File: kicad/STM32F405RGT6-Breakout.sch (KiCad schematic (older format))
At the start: 51 parts, among them J1 USB_C_Receptacle_USB2.0, J2 PWR OUT, J3 SWD/JTAG, J4 USART6, J5 SPI1, J6 I2C1, J7 I2C2, Q1 Si2301CDS, U1 STM32F405RGT6, U2 AMS1117-3.3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

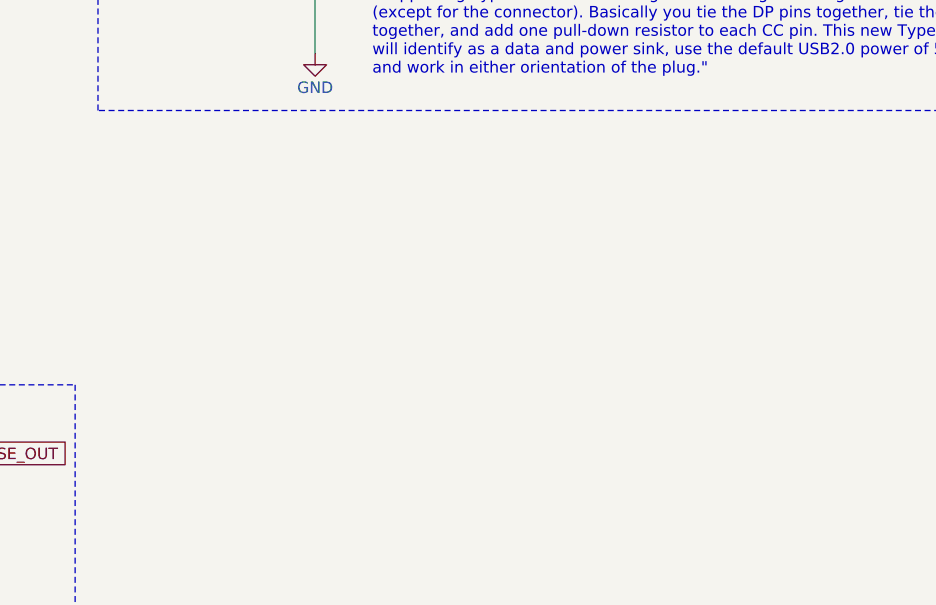
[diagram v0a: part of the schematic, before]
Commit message: clarify what software the board files are for
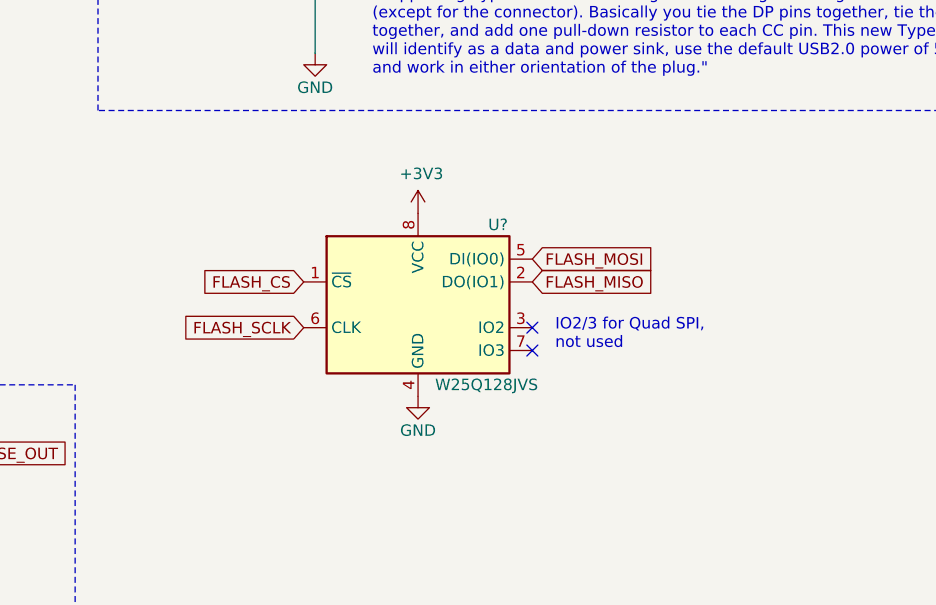
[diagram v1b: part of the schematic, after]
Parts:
- added U?: W25Q128JVS, Package_SO:SOIC-8_5.23x5.23mm_P1.27mm, symbol Memory_Flash:W25Q128JVS
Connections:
- net labels added: FLASH_CS, FLASH_MISO, FLASH_MOSI, FLASH_SCLK
- no-connect marks 37 -> 39
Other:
- note added: "IO2/3 for Quad SPI,\nnot used"
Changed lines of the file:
@@
 Wire Wire Line
 	2500 1350 2900 1350
+$Comp
+L Memory_Flash:W25Q128JVS U?
+U 1 1 61978862
+P 7500 6050
+F 0 "U?" H 7850 6400 50  0000 C CNN
+F 1 "W25Q128JVS" H 7800 5700 50  0000 C CNN
+F 2 "Package_SO:SOIC-8_5.23x5.23mm_P1.27mm" H 7500 6050 50  0001 C CNN
+F 3 "http://www.winbond.com/resource-files/w25q128jv_dtr%20revc%2003272018%20plus.pdf" H 7500 6050 50  0001 C CNN
+	1    7500 6050
+	1    0    0    -1
+$EndComp
+$Comp
+L power:GND #PWR?
+U 1 1 6197D247
+P 7500 6450
+F 0 "#PWR?" H 7500 6200 50  0001 C CNN
+F 1 "GND" H 7500 6300 50  0000 C CNN
+F 2 "" H 7500 6450 50  0001 C CNN
+F 3 "" H 7500 6450 50  0001 C CNN
+	1    7500 6450
+	1    0    0    -1
+$EndComp
+$Comp
+L power:+3V3 #PWR?
+U 1 1 6197DBCF
+P 7500 5650
+F 0 "#PWR?" H 7500 5500 50  0001 C CNN
+F 1 "+3V3" H 7515 5823 50  0000 C CNN
+F 2 "" H 7500 5650 50  0001 C CNN
+F 3 "" H 7500 5650 50  0001 C CNN
+	1    7500 5650
+	1    0    0    -1
+$EndComp
+Text GLabel 7000 5950 0    50   Input ~ 0
+FLASH_CS
+Text GLabel 7000 6150 0    50   Input ~ 0
+FLASH_SCLK
+Text GLabel 8000 5850 2    50   Input ~ 0
+FLASH_MOSI
+Text GLabel 8000 5950 2    50   Input ~ 0
+FLASH_MISO
+NoConn ~ 8000 6150
+NoConn ~ 8000 6250
+Text Notes 8100 6250 0    50   ~ 0
+IO2/3 for Quad SPI,\nnot used
 $EndSCHEMATC

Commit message: - Added onboard SPI flash, just to experiment with (128mb NOR flash is basic part at JLCPCB) - Added momentary switches for BOOT0 and NRST to get into DFU mode, like the black pill - Added a capacitor on NRST to avoid parasitic resets
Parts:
- removed R7: 10k, symbol Device:R_Small
- added C?: 0.1u, symbol Device:C_Small
- added C?: 4.7u, Capacitor_SMD:C_0805_2012Metric, symbol Device:C_Small
- added C?: 0.1u, Capacitor_SMD:C_0603_1608Metric, symbol Device:C_Small
- added R? (x6): 10k, symbol Device:R_Small
- added SW?: BOOT0 Momentary, symbol Switch:SW_Push_SPDT
- added SW?: NRST Momentary, symbol Switch:SW_Push_SPDT
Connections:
- net labels added: FLASH_SCK
- net labels removed: FLASH_SCLK
- wire segments 134 -> 153
- no-connect marks 39 -> 34
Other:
- note added: "(internal pullup)"
- note added: "Boot mode selection\n"
- note added: "Power supply"
- note added: "Quad\nSPI\nnot\nused"
- note added: "SPI Flash"
- note removed: "IO2/3 for Quad SPI,\nnot used"
- note removed: "Set boot mode"
- moved on the sheet: C14, C15, FB2, R3, R4, R5, R6, R8, U?

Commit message: Half way done with footprint assignment
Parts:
- removed F1: 500mA, symbol Device:Fuse_Small
- added F?: 500mA, symbol Device:Polyfuse_Small
- C16: footprint (none) -> Capacitor_SMD:C_1206_3216Metric
- C17: footprint (none) -> Capacitor_SMD:C_0805_2012Metric
- C18: renamed from C?; value 0.1u -> 100n; footprint (none) -> Capacitor_SMD:C_0402_1005Metric
- C19: renamed from C?; value 0.1u -> 100n
- D1: footprint (none) -> Diode_SMD:D_MiniMELF
- D2, D3: footprint (none) -> Diode_SMD:D_0603_1608Metric
- FB1, FB2: footprint (none) -> Inductor_SMD:L_0805_2012Metric
- H1, H2, H3, H4: footprint MountingHole:MountingHole_3mm_Pad_Via -> MountingHole:MountingHole_4.3mm_M4_Pad_Via
- J2: footprint (none) -> Connector_PinHeader_2.54mm:PinHeader_1x02_P2.54mm_Vertical_SMD_Pin1Left
- J3: footprint (none) -> Connector_PinSocket_1.27mm:PinSocket_2x05_P1.27mm_Vertical_SMD
- J4, J5, J6, J7: footprint (none) -> Connector_PinHeader_2.54mm:PinHeader_1x04_P2.54mm_Vertical_SMD_Pin1Left
- gave numbers to parts that had none: 10
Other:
- note removed: "Fuse\n(does this go \nbefore or \nafter pch?)"
- moved on the sheet: D1, Q1, R1

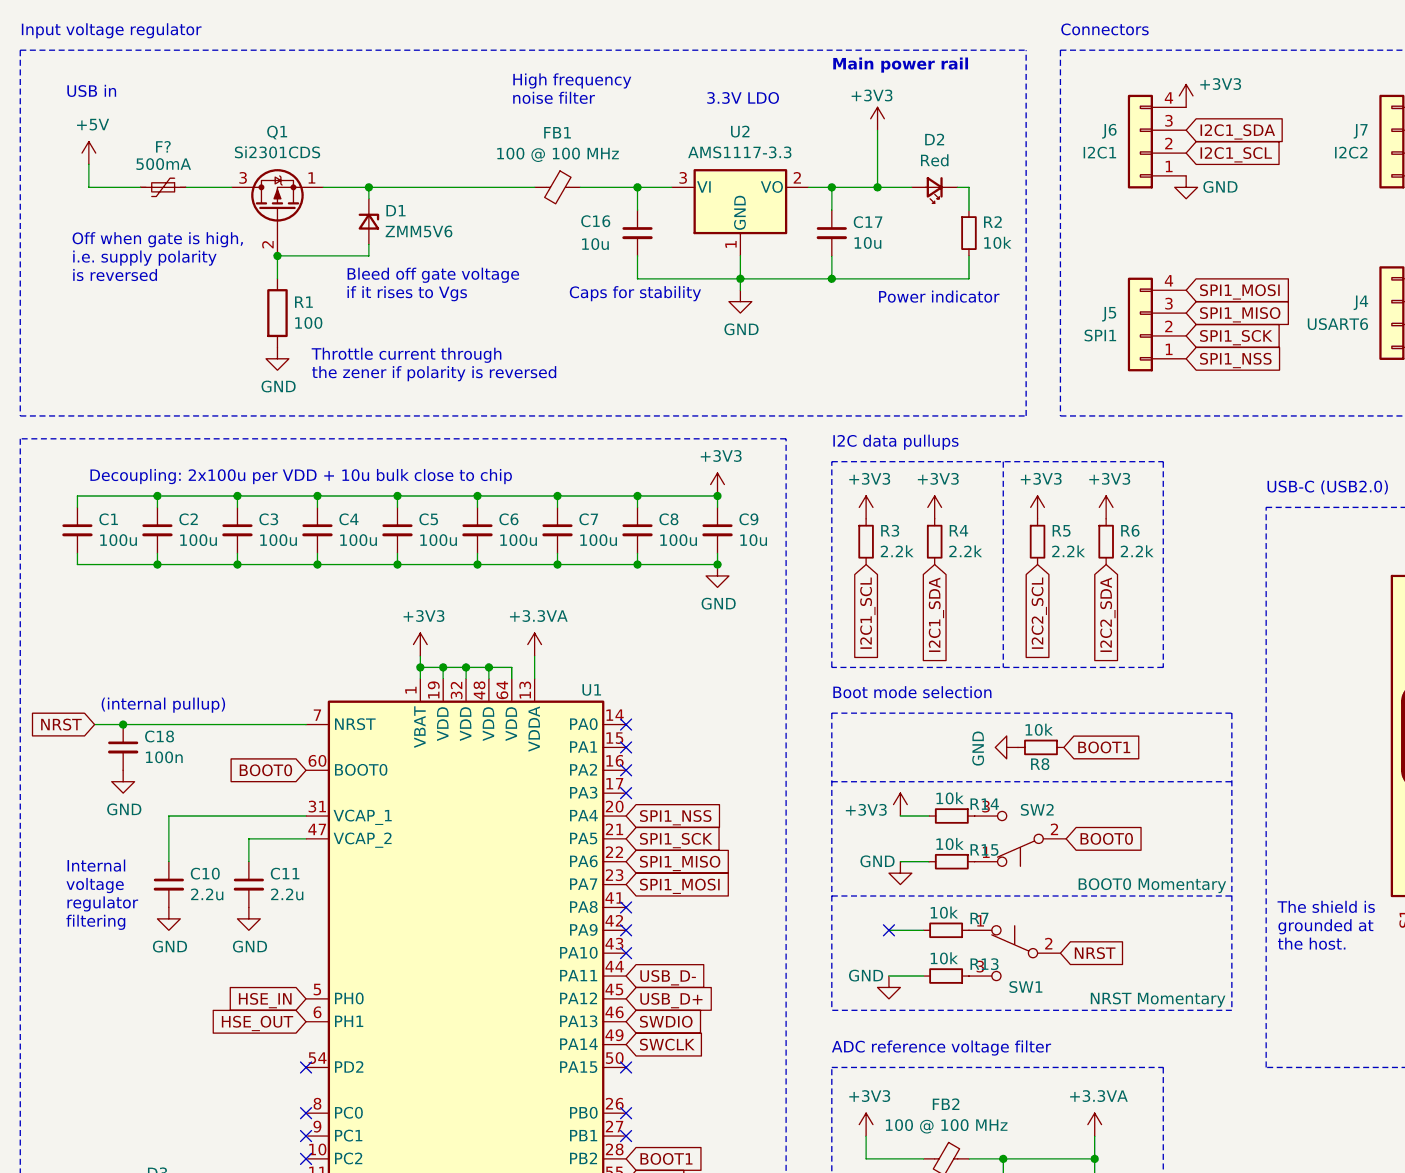
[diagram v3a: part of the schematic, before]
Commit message: - Added SPST tact switch symbol & footprint from JLPCB - Used SPST to ground NRST for reset - Used SPST to raise BOOT0 for DFU - BOOT0 on voltage divider, should work with the switch bringing BOOT0 to >2.2V (min high level 1.88V)
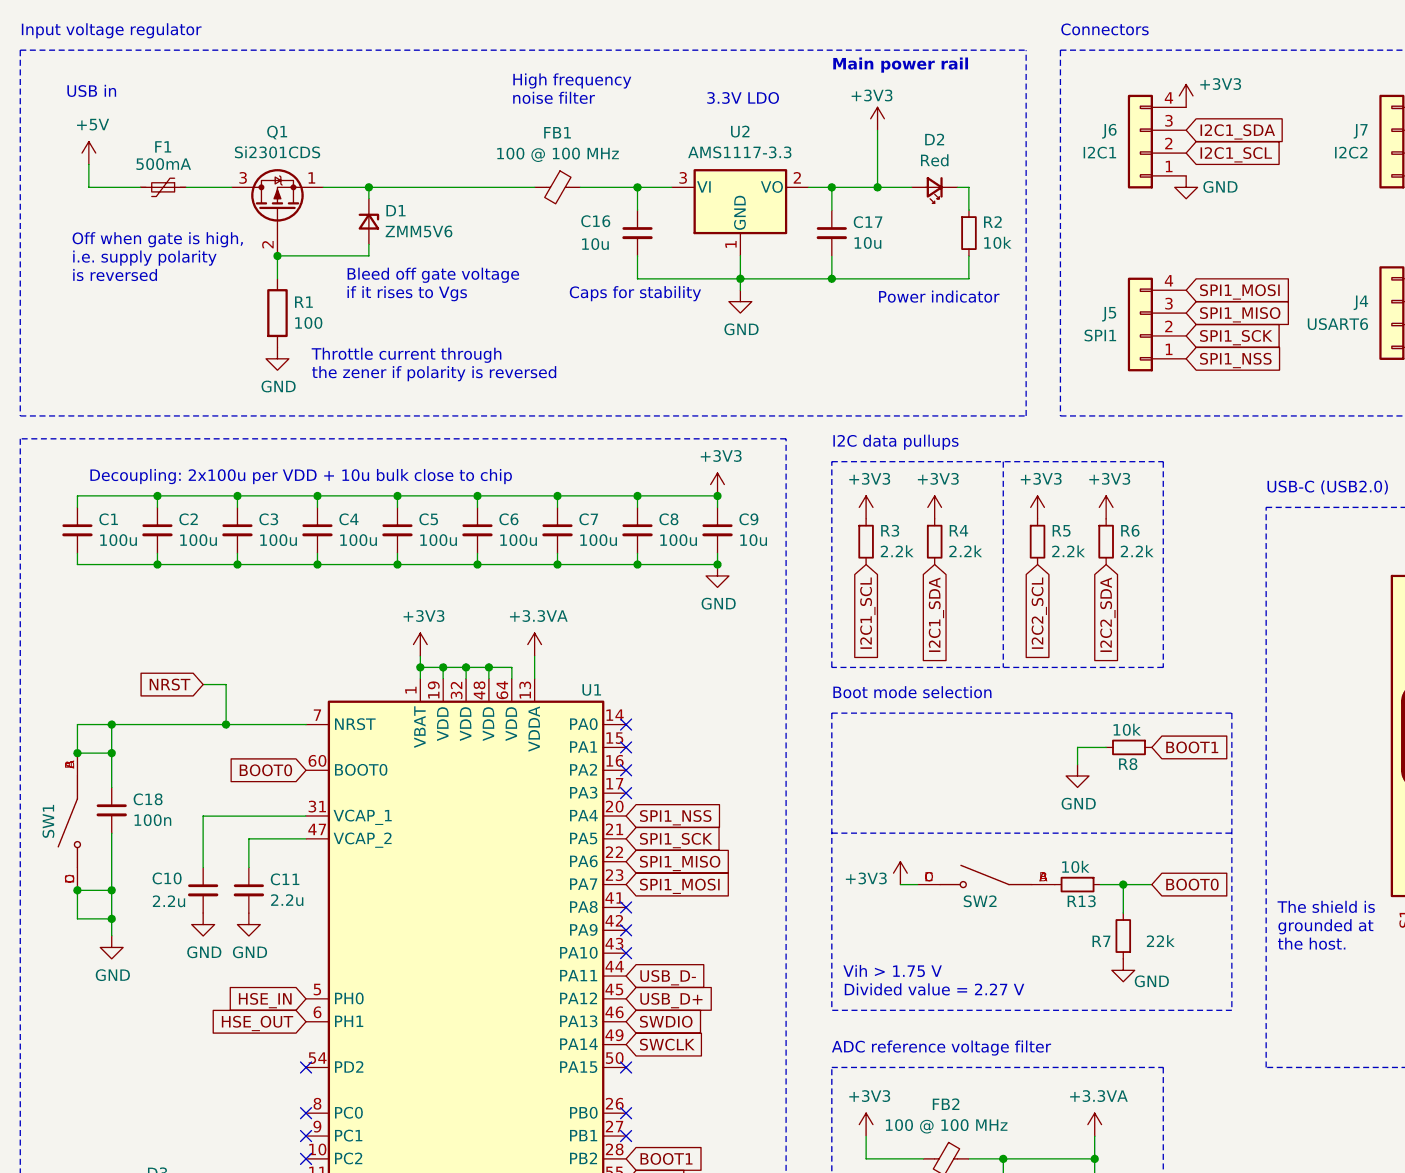
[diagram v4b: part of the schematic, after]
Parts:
- removed R14, R15: 10k, symbol Device:R_Small
- removed SW1: NRST Momentary, symbol Switch:SW_Push_SPDT
- removed SW2: BOOT0 Momentary, symbol Switch:SW_Push_SPDT
- added SW1, SW2: TS-1187A-B-A-B, TS-1187A-B-A-B:SW_TS-1187A-B-A-B, symbol TS-1187A-B-A-B:TS-1187A-B-A-B
- C1, C12, C13, C14, C15, C2, C3, C4, C5, C6, C7, C8: footprint (none) -> Capacitor_SMD:C_0402_1005Metric
- C10, C11, C9: footprint (none) -> Capacitor_SMD:C_0603_1608Metric
- C16: footprint Capacitor_SMD:C_1206_3216Metric -> Capacitor_SMD:C_0805_2012Metric
- F1: renamed from F?; footprint (none) -> Fuse:Fuse_0603_1608Metric
- FB1, FB2: JLCPCB Part (none) -> C1015
- HSE1: JLCPCB Part (none) -> C160456
- J1: JLCPCB Part (none) -> C319148
- Q1: footprint (none) -> Package_TO_SOT_SMD:SOT-23; JLCPCB Part (none) -> C10487
- R1: footprint (none) -> Resistor_SMD:R_0805_2012Metric
- R10, R11, R12, R13, R16, R17, R3, R4, R5, R6, R8: footprint (none) -> Resistor_SMD:R_0402_1005Metric
- R2, R9: footprint (none) -> Resistor_SMD:R_0603_1608Metric
- R7: value 10k -> 22k; footprint (none) -> Resistor_SMD:R_0603_1608Metric
- U1: JLCPCB Part (none) -> C15742
- U2: JLCPCB Part (none) -> C6186
- U3: JLCPCB Part (none) -> C2827654
- U4: JLCPCB Part (none) -> C97521
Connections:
- net +3V3: now also SW2.C, SW2.D
- net BOOT0: now also R13.1, R7.2
- net GND: now also R7.1, SW1.C, SW1.D; no longer R13.2
- net NRST: now also SW1.A, SW1.B
- new net: R13.2, SW2.A, SW2.B
- no-connect marks 34 -> 33
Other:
- note added: "Vih > 1.75 V\nDivided value = 2.27 V"
- note removed: "(internal pullup)"
- note removed: "Internal\nvoltage\nregulator\nfiltering"
- moved on the sheet: C10, C11, C18, R8

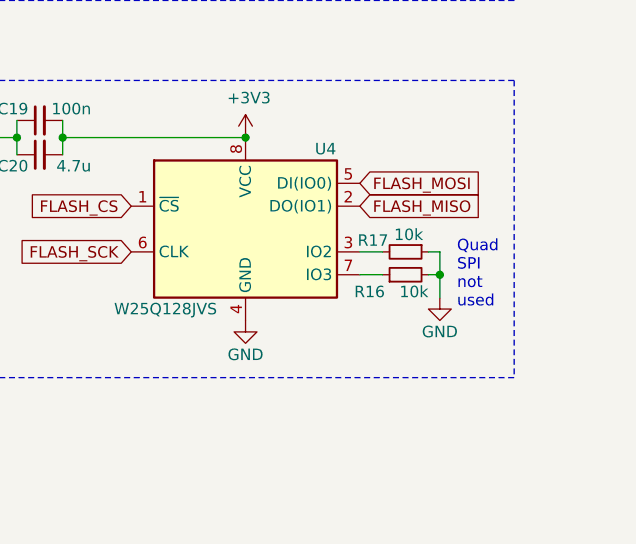
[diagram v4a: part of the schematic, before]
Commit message: - Laid out & routed crystal - Laid out & started routing MCU decoupling
--> Checkpoint before trying new flash orientation
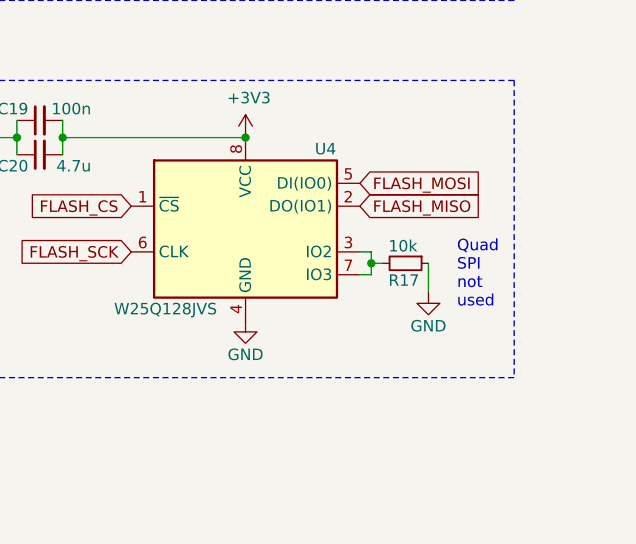
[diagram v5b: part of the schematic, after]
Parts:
- removed R16: 10k, Resistor_SMD:R_0402_1005Metric, symbol Device:R_Small
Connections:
- net GND: now also R17.1; no longer R17.2
- net at U4.3 (IO2): now also R17.2, U4.7 (IO3)
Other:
- moved on the sheet: R17
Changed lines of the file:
@@
 Quad\nSPI\nnot\nused
-$Comp
-L Device:R_Small R16
-U 1 1 6199EE81
-P 10275 6300
-F 0 "R16" V 10450 6075 50  0000 L CNN
-F 1 "10k" V 10200 6250 50  0000 L CNN
-F 2 "Resistor_SMD:R_0402_1005Metric" H 10275 6300 50  0001 C CNN
-F 3 "~" H 10275 6300 50  0001 C CNN
-	1    10275 6300
-	0    1    1    0
-$EndComp
-Wire Wire Line
-	10075 6300 10175 6300
 $Comp
 L power:GND #PWR0104
 U 1 1 619AB58F
-P 10425 6500
-F 0 "#PWR0104" H 10425 6250 50  0001 C CNN
-F 1 "GND" H 10425 6350 50  0000 C CNN
-F 2 "" H 10425 6500 50  0001 C CNN
-F 3 "" H 10425 6500 50  0001 C CNN
-	1    10425 6500
+P 10375 6475
+F 0 "#PWR0104" H 10375 6225 50  0001 C CNN
+F 1 "GND" H 10375 6325 50  0000 C CNN
+F 2 "" H 10375 6475 50  0001 C CNN
+F 3 "" H 10375 6475 50  0001 C CNN
+	1    10375 6475
 	1    0    0    -1
 $EndComp
@@
 L Device:R_Small R17
 U 1 1 6199FF9F
-P 10275 6400
-F 0 "R17" V 10425 6475 50  0000 L CNN
-F 1 "10k" V 10200 6300 50  0000 L CNN
-F 2 "Resistor_SMD:R_0402_1005Metric" H 10275 6400 50  0001 C CNN
-F 3 "~" H 10275 6400 50  0001 C CNN
-	1    10275 6400
-	0    -1   -1   0
-$EndComp
-Wire Wire Line
-	10375 6300 10425 6300
-Wire Wire Line
-	10425 6300 10425 6400
-Wire Wire Line
-	10375 6400 10425 6400
-Connection ~ 10425 6400
-Wire Wire Line
-	10425 6400 10425 6500
-Wire Wire Line
-	10175 6400 10075 6400
+P 10275 6350
+F 0 "R17" V 10350 6275 50  0000 L CNN
+F 1 "10k" V 10200 6275 50  0000 L CNN
+F 2 "Resistor_SMD:R_0402_1005Metric" H 10275 6350 50  0001 C CNN
+F 3 "~" H 10275 6350 50  0001 C CNN
+	1    10275 6350
+	0    1    1    0
+$EndComp
 Wire Notes Line
 	10750 5550 10750 6850
@@
 Text Notes 4250 4900 0    50   ~ 0
 Vih > 1.75 V\nDivided value = 2.27 V
+Wire Wire Line
+	10075 6300 10125 6300
+Wire Wire Line
+	10075 6400 10125 6400
+Wire Wire Line
+	10375 6350 10375 6475
+Wire Wire Line
+	10125 6300 10125 6350
+Wire Wire Line
+	10125 6350 10175 6350
+Connection ~ 10125 6350
+Wire Wire Line
+	10125 6350 10125 6400
 $EndSCHEMATC

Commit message: - USB connector & ESD protection laid out - Crystal moved to make room for fanning out GPIO pins
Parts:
- removed R12: 5.1k, Resistor_SMD:R_0402_1005Metric, symbol Device:R_Small
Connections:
- net at J1.A5 (CC1), R11.2: now also J1.B5 (CC2)
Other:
- moved on the sheet: R11
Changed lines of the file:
@@
 "Supporting Type-C from an existing USB2.0 design is straightforward and cheap \n(except for the connector). Basically you tie the DP pins together, tie the DM pins \ntogether, and add one pull-down resistor to each CC pin. This new Type-C device \nwill identify as a data and power sink, use the default USB2.0 power of 500 mA, \nand work in either orientation of the plug."
 Wire Wire Line
-	7650 3350 7700 3350
-Wire Wire Line
-	7650 3450 7700 3450
-Wire Wire Line
-	7900 3350 8300 3350
+	7650 3350 7750 3350
+Wire Wire Line
+	7650 3450 7750 3450
+Wire Wire Line
+	8075 3350 8300 3350
 Wire Wire Line
 	8300 3350 8300 3450
-Wire Wire Line
-	8300 3450 7900 3450
 $Comp
 L power:GND #PWR037
@@
 	1    0    0    -1
 $EndComp
-Connection ~ 8300 3450
 Wire Wire Line
 	7700 3750 7650 3750
@@
 L Device:R_Small R11
 U 1 1 61FB8501
-P 7800 3350
-F 0 "R11" V 7750 3500 50  0000 C CNN
-F 1 "5.1k" V 7700 3350 50  0000 C CNN
-F 2 "Resistor_SMD:R_0402_1005Metric" H 7800 3350 50  0001 C CNN
-F 3 "~" H 7800 3350 50  0001 C CNN
-	1    7800 3350
+P 7975 3350
+F 0 "R11" V 7925 3500 50  0000 C CNN
+F 1 "5.1k" V 7875 3350 50  0000 C CNN
+F 2 "Resistor_SMD:R_0402_1005Metric" H 7975 3350 50  0001 C CNN
+F 3 "~" H 7975 3350 50  0001 C CNN
+	1    7975 3350
 	0    1    1    0
 $EndComp
@@
 	1    4650 2900
 	1    0    0    -1
-$EndComp
-$Comp
-L Device:R_Small R12
-U 1 1 61FB9709
-P 7800 3450
-F 0 "R12" V 7850 3600 50  0000 C CNN
-F 1 "5.1k" V 7900 3450 50  0000 C CNN
-F 2 "Resistor_SMD:R_0402_1005Metric" H 7800 3450 50  0001 C CNN
-F 3 "~" H 7800 3450 50  0001 C CNN
-	1    7800 3450
-	0    1    1    0
 $EndComp
 Text Notes 7750 4400 0    50   ~ 0
@@
 Wire Wire Line
 	10125 6350 10125 6400
+Wire Wire Line
+	7750 3350 7750 3450
+Connection ~ 7750 3350
+Wire Wire Line
+	7750 3350 7875 3350
 $EndSCHEMATC
